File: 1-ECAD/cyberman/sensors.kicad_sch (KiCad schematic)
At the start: 7 parts, among them U11 LSM6DSOTR, U12 LIS2MDLTR

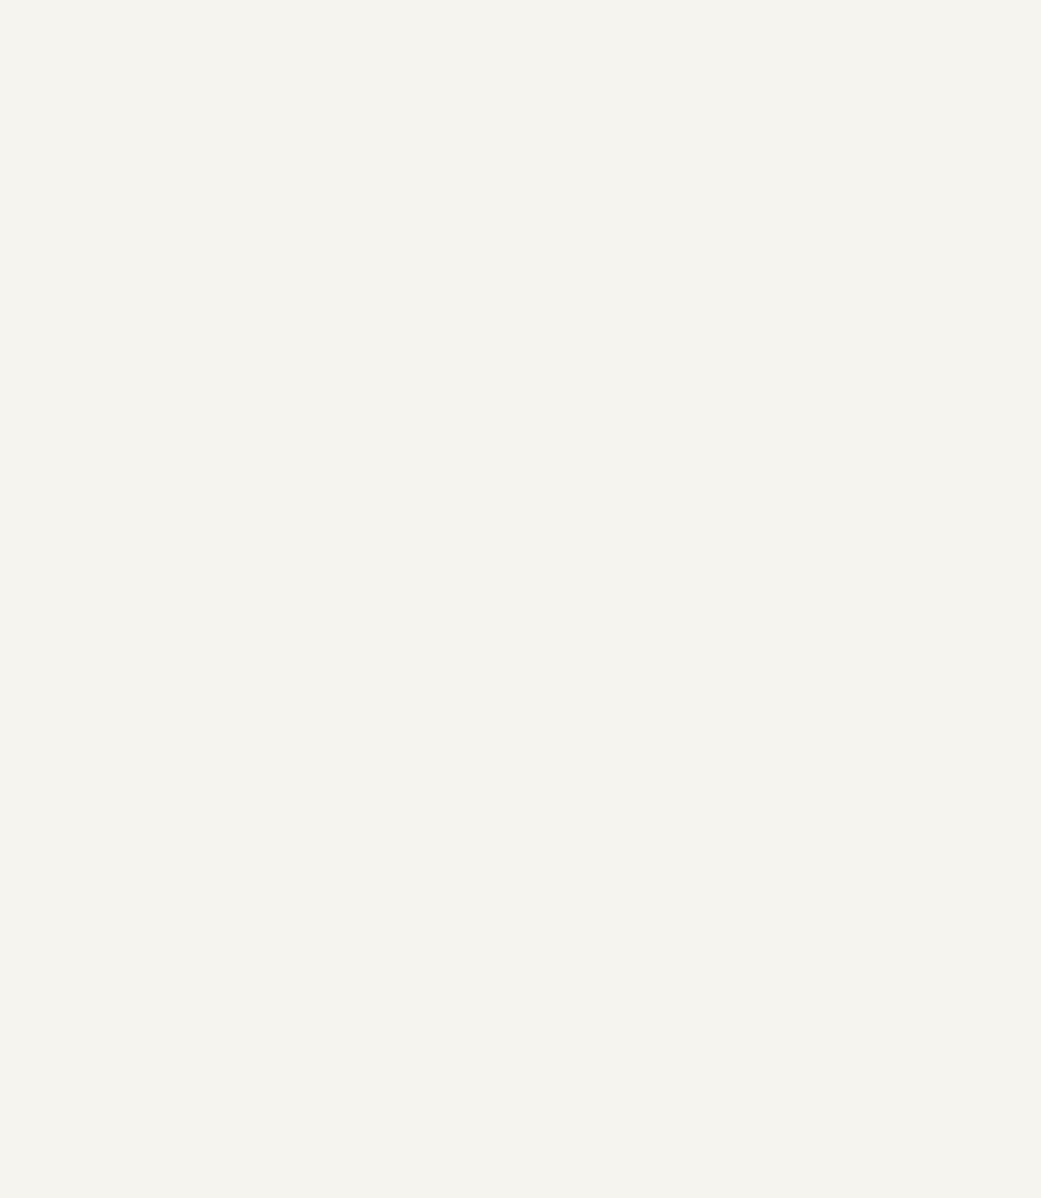
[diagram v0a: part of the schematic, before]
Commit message: add mic and speaker
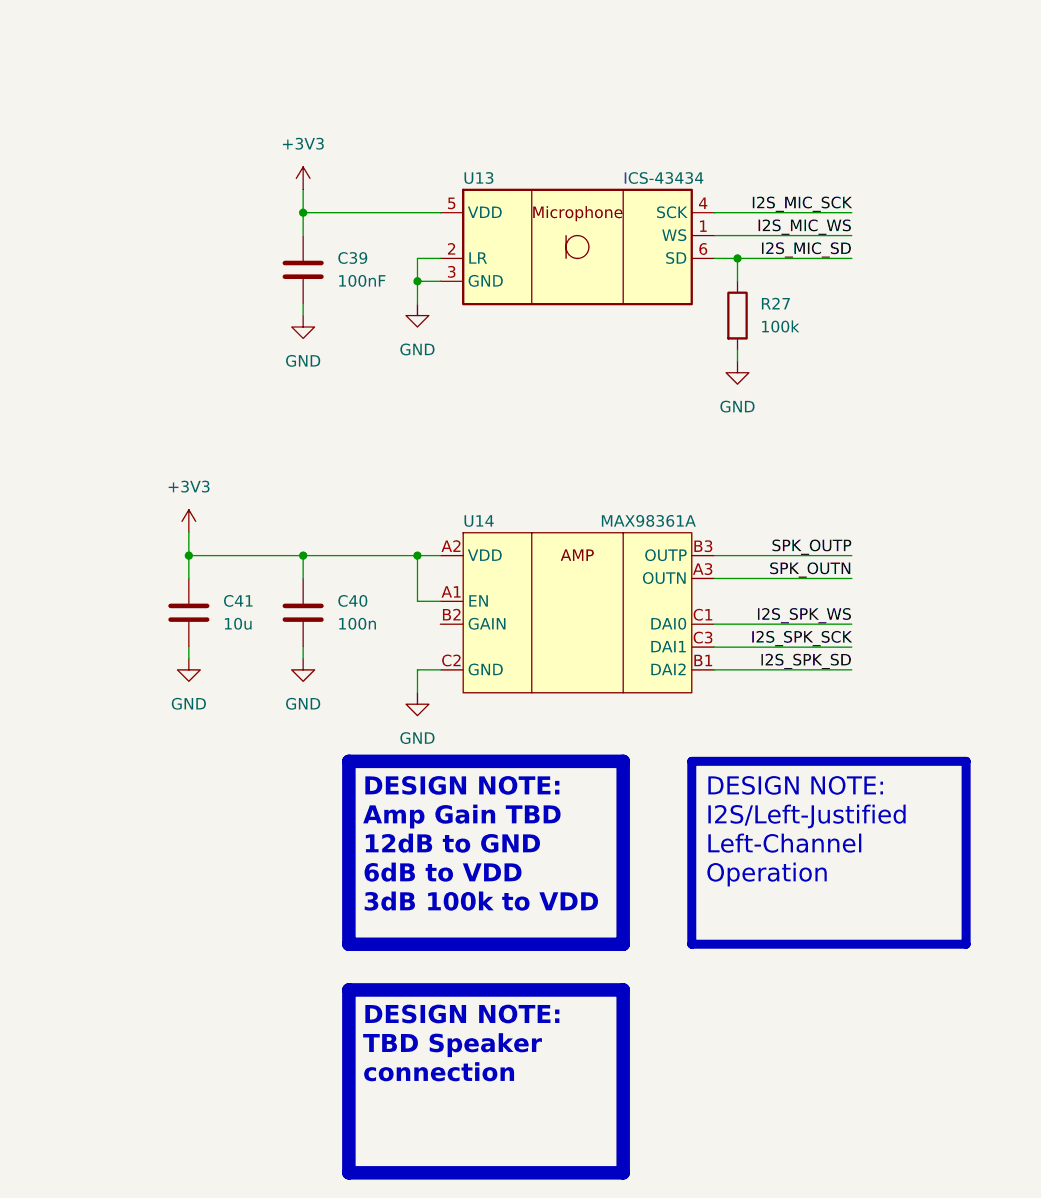
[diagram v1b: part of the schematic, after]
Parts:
- added C39: 100nF, symbol Device:C
- added C40: 100n, symbol Device:C
- added C41: 10u, symbol Device:C
- added R27: 100k, symbol Device:R
- added U13: ICS-43434, symbol 0_sensor:ICS-43434
- added U14: MAX98361A, symbol 0_CI_smd:MAX98361A
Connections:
- net +3V3: now also C39.1, C40.1, C41.1, U13.5 (VDD), U14.A1 (EN), U14.A2 (VDD)
- net GND: now also C39.2, C40.2, C41.2, R27.2, U13.2 (LR), U13.3 (GND), U14.C2 (GND)
- new net I2S_MIC_SCK: U13.4 (SCK)
- new net I2S_MIC_SD: R27.1, U13.6 (SD)
- new net I2S_MIC_WS: U13.1 (WS)
- new net I2S_SPK_SCK: U14.C3 (DAI1)
- new net I2S_SPK_SD: U14.B1 (DAI2)
- new net I2S_SPK_WS: U14.C1 (DAI0)
- new net SPK_OUTN: U14.A3 (OUTN)
- new net SPK_OUTP: U14.B3 (OUTP)

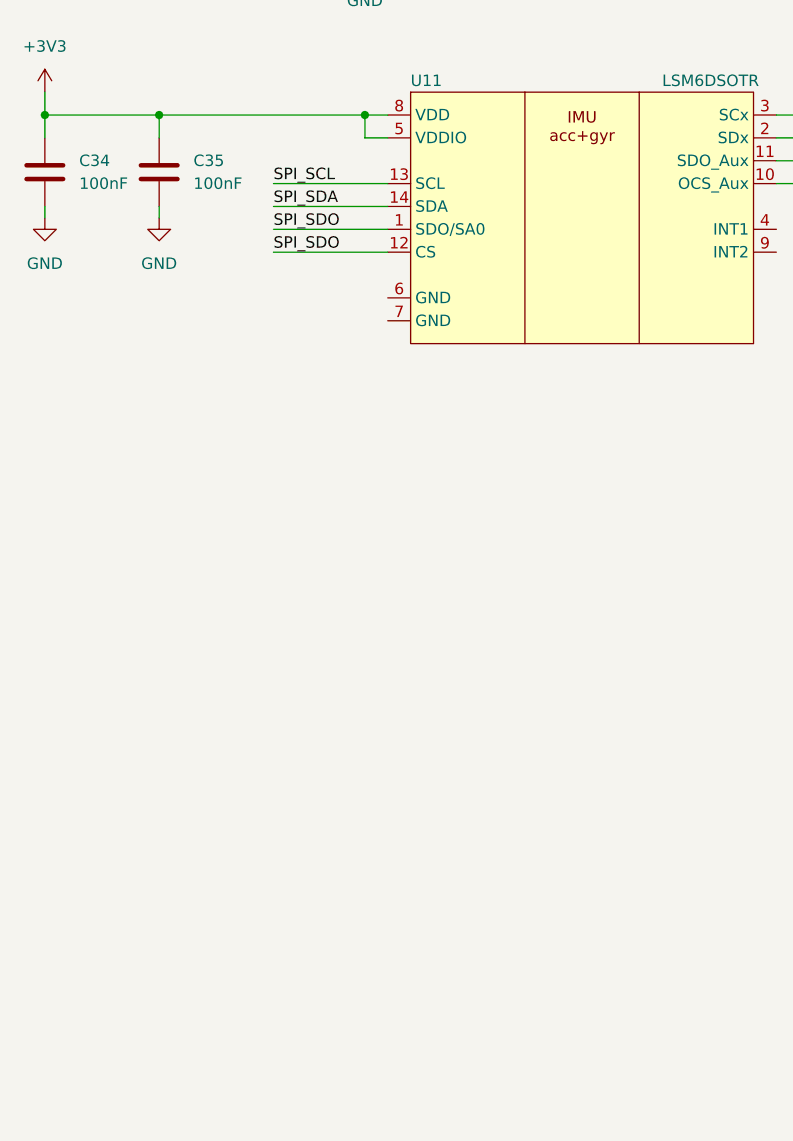
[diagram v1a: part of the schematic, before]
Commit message: add bus and display connection
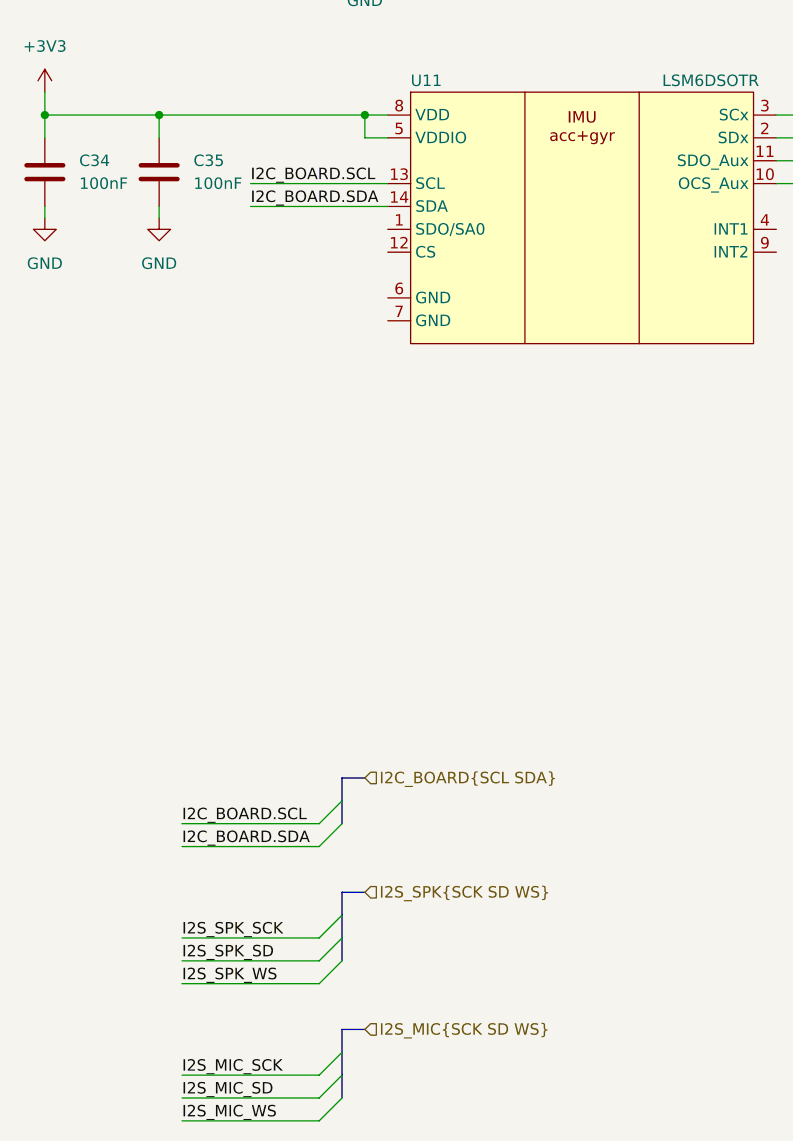
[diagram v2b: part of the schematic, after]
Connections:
- net SPI_SCL renamed I2C_BOARD.SCL
- net SPI_SDA renamed I2C_BOARD.SDA
- net SPI_SDO: no longer names the net of U11.1 (SDO/SA0)
- net SPI_SDO: no longer U11.12 (CS)

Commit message: hey
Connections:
- net I2S_SPK_SCK is gone; now on net I2S.SCK: U14.C3 (DAI1)
- net I2S_SPK_SD is gone; now on net I2S.SD: U14.B1 (DAI2)
- net I2S_SPK_WS is gone; now on net I2S.WS: U14.C1 (DAI0)
- net GND: now also U11.6 (GND), U11.7 (GND)
- net I2S_MIC_SCK renamed I2S.SCK
- net I2S_MIC_SD renamed I2S.SD
- net I2S_MIC_WS renamed I2S.WS

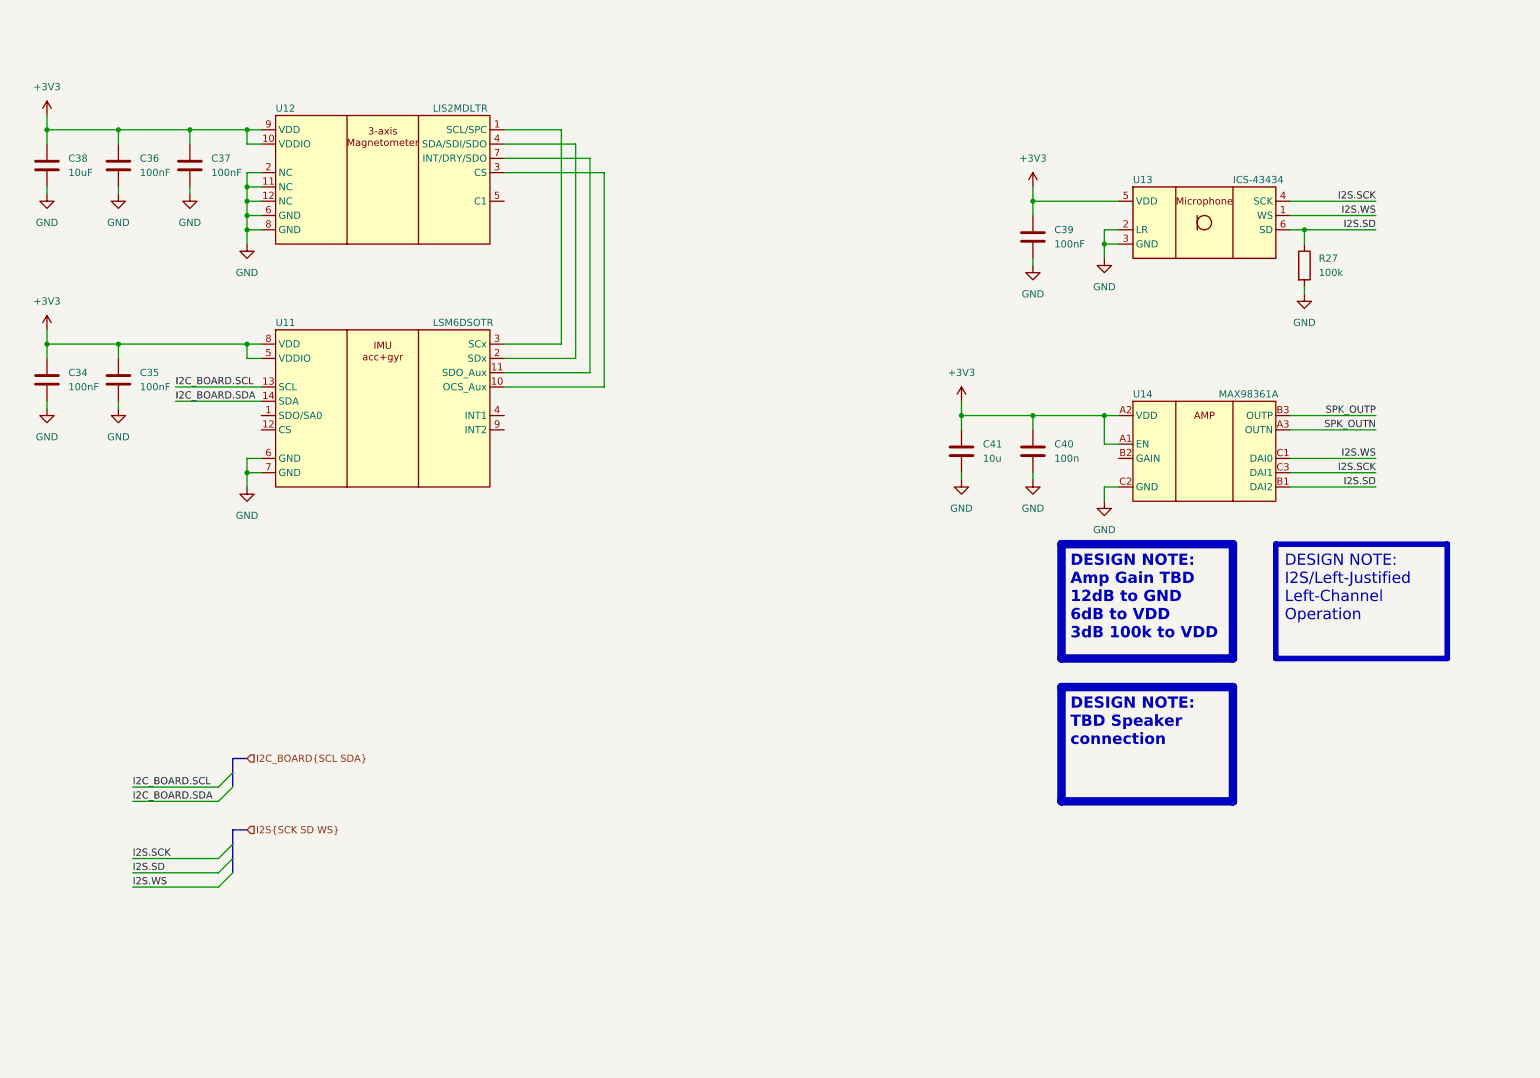
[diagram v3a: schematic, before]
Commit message: add expander io and pic
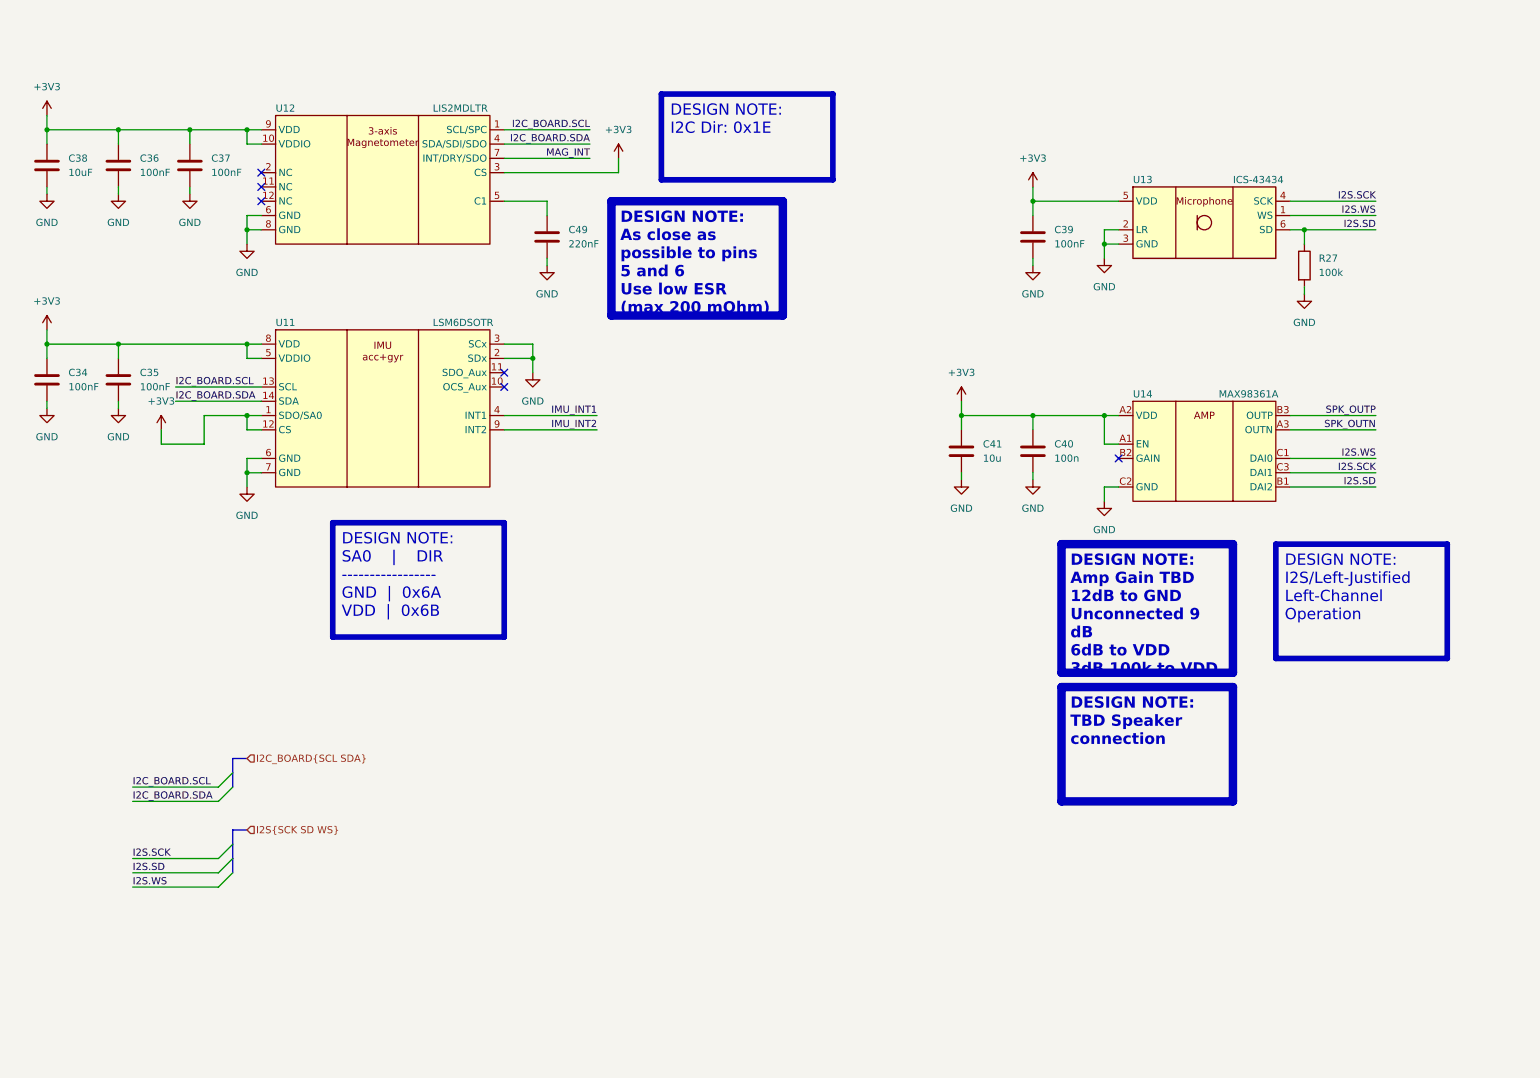
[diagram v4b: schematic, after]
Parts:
- added C49: 220nF, symbol Device:C
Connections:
- net +3V3: now also U11.1 (SDO/SA0), U11.12 (CS), U12.3 (CS)
- net GND: now also U11.2 (SDx), U11.3 (SCx), C49.2; no longer U12.11 (NC), U12.12 (NC), U12.2 (NC)
- net I2C_BOARD.SCL: now also U12.1 (SCL/SPC)
- net I2C_BOARD.SDA: now also U12.4 (SDA/SDI/SDO)
- net at U11.10 (OCS_Aux): no longer U12.3 (CS)
- net at U12.5 (C1): now also C49.1
- net at U11.11 (SDO_Aux): no longer U12.7 (INT/DRY/SDO)
- net IMU_INT1: now reaches U11.4 (INT1)
- net IMU_INT2: now reaches U11.9 (INT2)
- new net MAG_INT: U12.7 (INT/DRY/SDO)
- no-connect marks 0 -> 6

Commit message: footpritn day
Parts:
- removed U12: LIS2MDLTR, symbol 0_sensor:LIS2MDLTR
- removed U13: ICS-43434, symbol 0_sensor:ICS-43434
- removed U14: MAX98361A, symbol 0_CI_smd:MAX98361A
- added C52, C53: 220pF, symbol Device:C
- added J3: 532610271, 0_connector_smd:532610271, symbol 0_connector_smd:532610271
- added L6, L7: BLM15PX331SZ1D, 0_inductor_smd:BLM15PX331SZ1D, symbol 0_inductor_smd:BLM15PX331SZ1D
- added U12: ICS-43434, 0_sensor:ICS-43434, symbol 0_sensor:ICS-43434
- added U13: MAX98357A, 0_CI_smd:MAX98357AETE+T, symbol 0_CI_smd:MAX98357A
- added U20: LIS2MDLTR, 0_sensor:LIS2MDLTR, symbol 0_sensor:LIS2MDLTR
- U11: footprint (none) -> 0_sensor:LSM6DSOTR
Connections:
- net +3V3: now also U12.5 (VDD), U13.7 (VDD), U13.8 (VDD), U20.10 (VDDIO), U20.3 (CS), U20.9 (VDD)
- net GND: now also C52.2, C53.2, J3.S1 (SHIELD1), J3.S2 (SHIELD2), U12.2 (LR), U12.3 (GND), U13.11 (GND), U13.15 (GND), U13.17 (EP), U13.3 (GND), U20.6 (GND), U20.8 (GND)
- net I2C_BOARD.SCL: now also U20.1 (SCL/SPC)
- net I2C_BOARD.SDA: now also U20.4 (SDA/SDI/SDO)
- net I2S.SCK: now also U12.4 (SCK), U13.16 (BCLK)
- net I2S.SD: now also U12.6 (SD), U13.1 (DIN)
- net I2S.WS: now also U12.1 (WS), U13.14 (LRCLK)
- net MAG_INT: now also U20.7 (INT/DRY/SDO)
- net at C49.1: now also U20.5 (C1)
- new net: L6.1, U13.9 (OUTP)
- new net: C53.1, J3.1 (Pin_1), L6.2
- new net: C52.1, J3.2 (Pin_2), L7.2
- new net: L7.1, U13.10 (OUTN)
- new net SPK_SD: U13.4 (~{SD_MODE})
- no-connect marks 6 -> 10
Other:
- moved on the sheet: C40, C41
